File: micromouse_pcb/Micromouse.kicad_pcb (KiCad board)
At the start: 4 copper layers, 117.6 x 85 mm, 85 parts, among them J1 Conn_01x06, J2 Conn_01x06, J3 SWD, J4 UART, Q1 NMOS, Q2 SFH300, Q3 SFH300, Q4 NMOS, Q5 SFH300, Q6 NMOS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

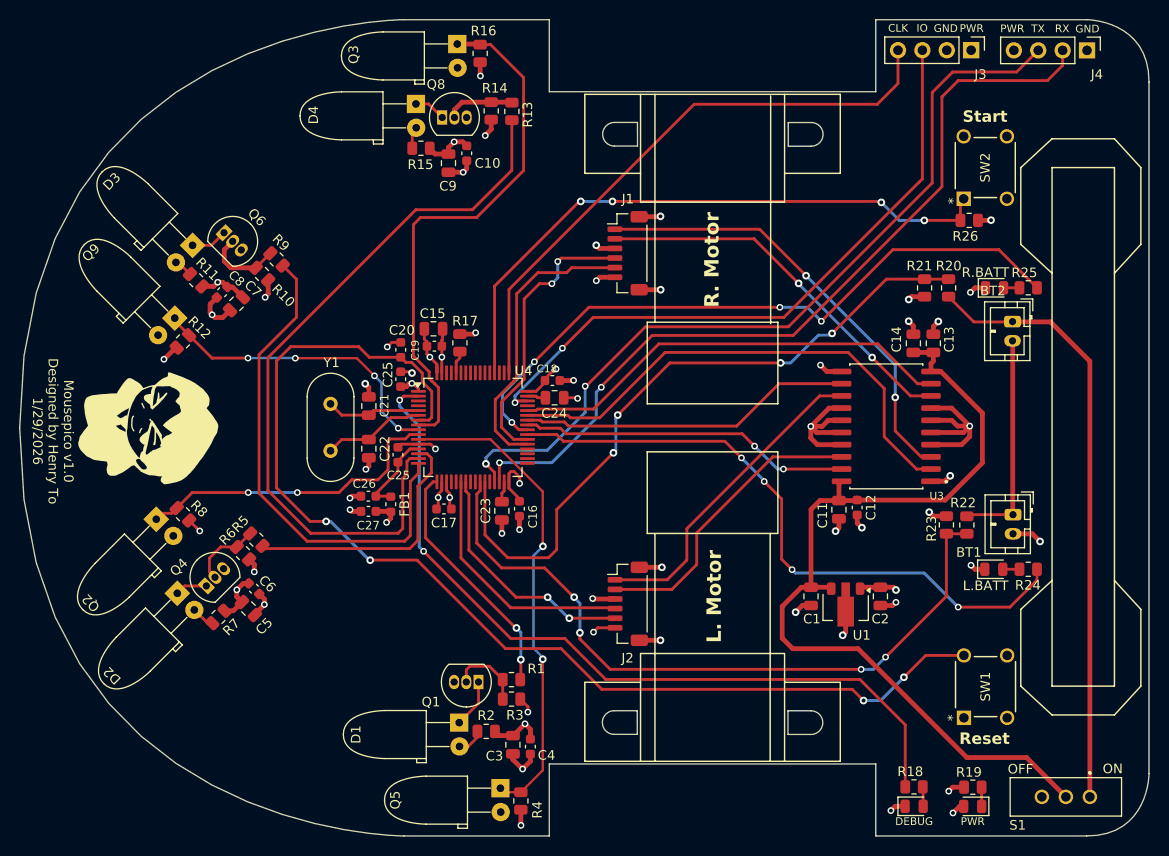
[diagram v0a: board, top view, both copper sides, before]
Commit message: v2 kicad micromouse started, and turning is now possible but please fix distance reading and distance pids
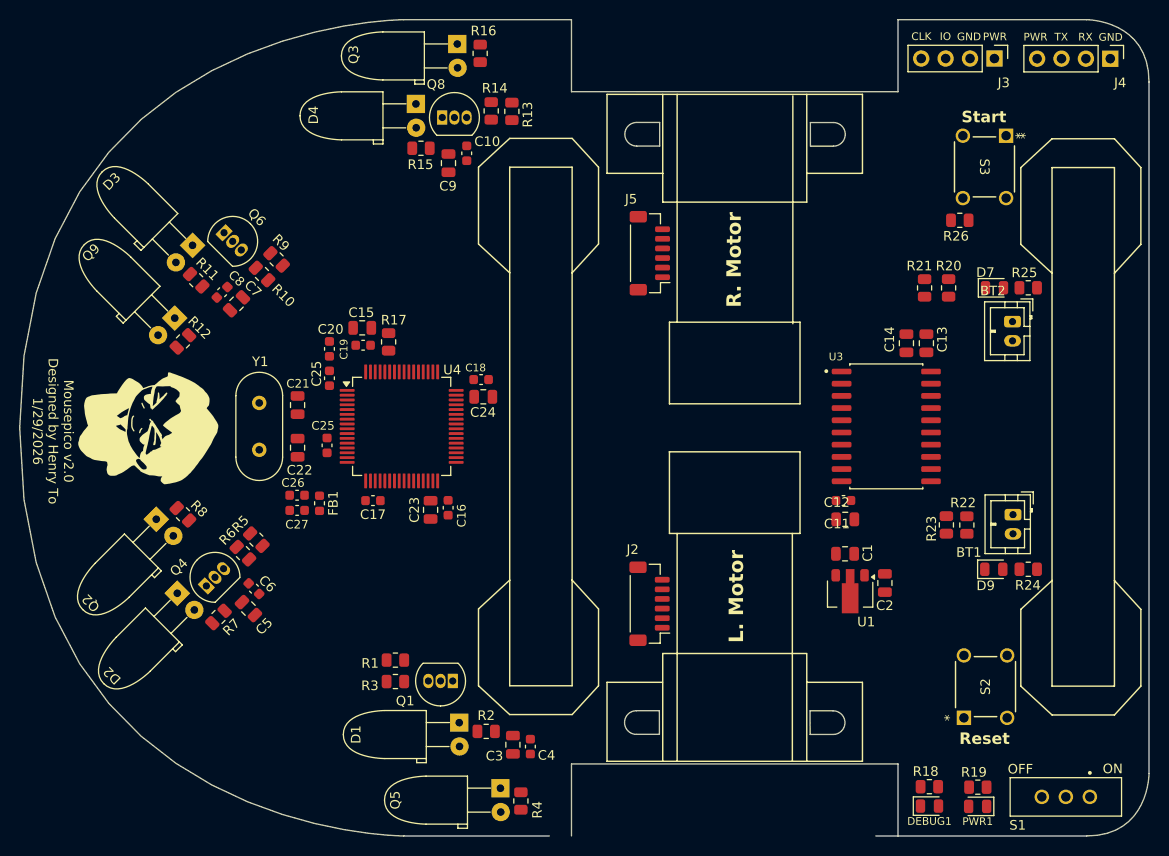
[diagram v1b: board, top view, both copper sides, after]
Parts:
- removed J1: Conn_01x06, Connector_JST:JST_SH_BM06B-SRSS-TB_1x06-1MP_P1.00mm_Vertical
- removed SW1, SW2: SW_Push, footprints:SW4_1825910-B_TEC
- added J5: Conn_01x06_MountingPin, Connector_JST:JST_SH_BM06B-SRSS-TB_1x06-1MP_P1.00mm_Vertical, F.Cu at (149.7, 69.5)
- added S2: FSM8JH, footprints:SW4_1825910-B_TEC, F.Cu at (186.9, 111.4)
- added S3: FSM8JH, footprints:SW4_1825910-B_TEC, F.Cu at (182.3, 63.7)
- J2: value Conn_01x06 -> Conn_01x06_MountingPin
- R12, R16, R4, R8: value 1k8 -> 2k
- R21: value 56k -> 60.4k
- R22: value 22k -> 20k
- moved R1 12.3 mm to (123.2, 111.8), turned to 0 degrees
- moved R3 12.2 mm to (123.2, 114.1), turned to 0 degrees
- moved C25 7.45 mm to (116.1, 89.5)
- moved C17 7.44 mm to (120.8, 95.2)
- moved C23 7.42 mm to (126.8, 96.2)
- moved C20 7.42 mm to (116.3, 79.4)
- moved C21 7.42 mm to (113.0, 85.3)
- moved C22 7.42 mm to (113.0, 89.7)
- moved C25 7.42 mm to (116.3, 82.5)
- moved C27 7.42 mm to (113.0, 96.3)
- moved FB1 7.42 mm to (115.3, 95.5)
- moved R17 7.42 mm to (122.5, 78.7)
- moved C15 7.42 mm to (119.7, 77.2)
- moved C16 7.42 mm to (128.7, 96.0)
- moved C18 7.42 mm to (132.1, 82.6)
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- renumbered R.BATT to D7, L.BATT to D9, DEBUG to DEBUG1, PWR to PWR1
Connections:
- BT1 pad 1: Net-(BT1--) -> GND
- BT1 pad 2: GND -> Net-(BT1--)
- BT2 pad 1: Net-(BT2--) -> Net-(BT1--)
- BT2 pad 2: Net-(BT1--) -> Net-(BT2--)
- J2 pad 1: MR_1 -> GND
- J2 pad 2: MR_2 -> EL_OUT2
- J2 pad 3: 3V3 -> EL_OUT1
- J2 pad 4: ER_OUT1 -> 3V3
- J2 pad 5: ER_OUT2 -> ML_2
- J2 pad 6: GND -> ML_1
- U4 pad 14: EM_3 -> EM_2
- U4 pad 16: EM_2 -> EM_3
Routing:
- net GND: track 131.9 -> 0.00 mm, vias 48 -> 0
- net Net-(U4-NRST): track 119.4 -> 0.00 mm, vias 4 -> 0
- net VDD: track 92.5 -> 0.00 mm
- net UART_RX: track 86.4 -> 0.00 mm, vias 2 -> 0
- net UART_TX: track 85.1 -> 0.00 mm, vias 2 -> 0
- net Net-(U4-PC13): track 83.0 -> 0.00 mm, vias 2 -> 0
- net EM_4: track 77.1 -> 0.00 mm
- net V2: track 74.9 -> 0.00 mm, vias 4 -> 0
- net V1: track 71.3 -> 0.00 mm, vias 4 -> 0
- net Net-(U4-PC9): track 70.1 -> 0.00 mm, vias 4 -> 0
- net SWDIO: track 67.3 -> 0.00 mm, vias 2 -> 0
- net Net-(U4-PC8): track 66.5 -> 0.00 mm, vias 4 -> 0
- net Start: track 64.4 -> 0.00 mm, vias 4 -> 0
- net Net-(BT2--): track 62.9 -> 0.00 mm
- net SWCLK: track 61.5 -> 0.00 mm
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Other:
- outline, holes or cut-outs redrawn
- board text added: "Mousepico v2.0 Designed by Henry To 1/29/2026"
- board text removed: "Mousepico v1.0 Designed by Henry To 1/29/2026"

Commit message: finished v2 micromouse, finished move function, todo: fix distance pid
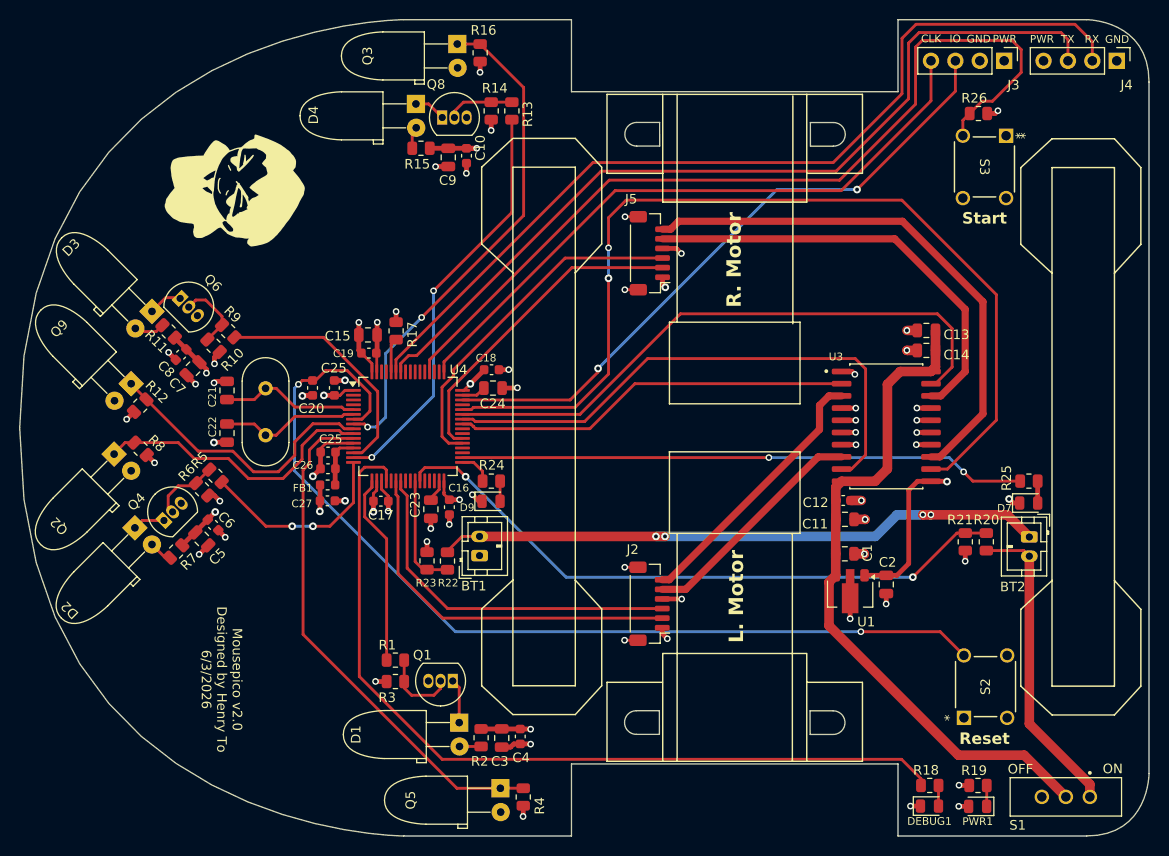
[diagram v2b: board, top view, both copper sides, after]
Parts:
- Q2, Q3, Q5, Q9: footprint LED_THT:led_micro -> micromouse:led_micro
- moved R24 56.7 mm to (133.2, 93.2), turned to 180 degrees
- moved BT1 55.7 mm to (131.9, 101.0), turned to 90 degrees
- moved R23 54.2 mm to (126.5, 101.5)
- moved R22 54.2 mm to (128.6, 101.5)
- moved D9 52.8 mm to (133.1, 95.3)
- moved R21 26.8 mm to (182.5, 99.5)
- moved R20 26.7 mm to (184.7, 99.5)
- moved G*** 26.3 mm to (106.5, 62.8)
- moved D7 22.7 mm to (189.1, 95.5)
- moved BT2 22.5 mm to (189.2, 99.0)
- moved R25 20.1 mm to (189.2, 93.2), turned to 180 degrees
- moved R26 11.3 mm to (183.9, 54.9)
- moved R10 9.01 mm to (104.3, 79.1)
- moved R9 9.01 mm to (105.8, 77.6)
- moved C5 8.73 mm to (103.0, 99.2)
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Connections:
- R18 pad 2: Net-(U4-PC13) -> Net-(U4-PA4)
- R24 pad 2: Net-(U4-PC8) -> Net-(U4-PB12)
- R25 pad 2: Net-(U4-PC9) -> Net-(U4-PB13)
- U4 pad 2: Net-(U4-PC13) -> unconnected-(U4-PC13-Pad2)
- U4 pad 20: unconnected-(U4-PA4-Pad20) -> Net-(U4-PA4)
- U4 pad 22: ER_OUT1 -> EL_OUT2
- U4 pad 23: ER_OUT2 -> EL_OUT1
- U4 pad 29: UART_TX -> unconnected-(U4-PB10-Pad29)
- U4 pad 30: UART_RX -> unconnected-(U4-PB11-Pad30)
- U4 pad 33: unconnected-(U4-PB12-Pad33) -> Net-(U4-PB12)
- U4 pad 34: unconnected-(U4-PB13-Pad34) -> Net-(U4-PB13)
- U4 pad 37: EL_OUT2 -> ER_OUT1
- U4 pad 38: EL_OUT1 -> ER_OUT2
- U4 pad 39: Net-(U4-PC8) -> unconnected-(U4-PC8-Pad39)
- U4 pad 40: Net-(U4-PC9) -> unconnected-(U4-PC9-Pad40)
- U4 pad 41: PWM4 -> PWM1
- U4 pad 42: PWM3 -> PWM2
- U4 pad 43: PWM1 -> PWM4
- U4 pad 44: PWM2 -> PWM3
- U4 pad 58: unconnected-(U4-PB6-Pad58) -> UART_TX
- U4 pad 59: unconnected-(U4-PB7-Pad59) -> UART_RX
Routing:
- net PWM3: track 0.00 -> 100.2 mm, vias 0 -> 2
- net Net-(U4-NRST): track 0.00 -> 99.8 mm, vias 0 -> 2
- net UART_RX: track 0.00 -> 94.4 mm
- net Start: track 0.00 -> 92.7 mm
- net UART_TX: track 0.00 -> 90.5 mm
- net Net-(U4-PA4): track 0.00 -> 89.1 mm
- net GND: track 0.00 -> 85.4 mm, vias 0 -> 55
- net VDD: track 0.00 -> 71.3 mm
- net SWDIO: track 0.00 -> 68.0 mm, vias 0 -> 2
- net 3V3: track 0.00 -> 67.9 mm, vias 0 -> 16
- net SWCLK: track 0.00 -> 67.2 mm
- net V1: track 0.00 -> 66.7 mm, vias 0 -> 2
- net Net-(BT1--): track 0.00 -> 65.1 mm, vias 0 -> 4
- net PWM4: track 0.00 -> 62.9 mm
- net Net-(U4-PB13): track 0.00 -> 59.1 mm, vias 0 -> 2
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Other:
- outline, holes or cut-outs redrawn
- board text added: "Mousepico v2.0 Designed by Henry To 6/3/2026"
- board text removed: "Mousepico v2.0 Designed by Henry To 1/29/2026"
